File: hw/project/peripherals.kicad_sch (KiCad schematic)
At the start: 72 parts, among them J1 Battery, J10 I2C, J11 Voltage Monitor, J12 Misc, J2 Phases, J3 FTSH-107-01-L-DV-K-A, J4 Throttle, J5 Hall, J6 Serial, J7 SPI, J8 2.54 Comm, J9 CAN, SW3 USER, U3 ATA6561-GAQW-N

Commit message: somewhat organize main groups
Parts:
- renumbered R44 to R38, R45 to R39, R46 to R40, R47 to R41, R48 to R42, R49 to R43, R50 to R44, R51 to R45, R52 to R46, R53 to R47, R54 to R48, R55 to R49, R56 to R50, R57 to R51, R58 to R52, R59 to R53, R60 to R54, R61 to R55, R62 to R56, R63 to R57, R64 to R58, R65 to R59, R66 to R60, R67 to R61, R68 to R62, R69 to R63
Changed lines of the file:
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@@
 		(dnp no)
 		(fields_autoplaced yes)
-		(property "Reference" "R48"
+		(property "Reference" "R42"
 			(at 260.35 38.0999 0)
 			(show_name no)
@@
 			(project "esc"
 				(path "/86a17c4d-db96-42a1-af84-d43fe593f4e6/84ea8536-46c8-4cae-8743-a6718dee2882"
-					(reference "R48")
+					(reference "R42")
 					(unit 1)
 				)
@@
 		(dnp no)
 		(fields_autoplaced yes)
-		(property "Reference" "R58"
+		(property "Reference" "R52"
 			(at 246.38 85.0899 0)
 			(show_name no)
@@
 			(project "esc"
 				(path "/86a17c4d-db96-42a1-af84-d43fe593f4e6/84ea8536-46c8-4cae-8743-a6718dee2882"
-					(reference "R58")
+					(reference "R52")
 					(unit 1)
 				)
@@
 		(dnp no)
 		(fields_autoplaced yes)
-		(property "Reference" "R44"
+		(property "Reference" "R38"
 			(at 246.38 30.4799 0)
 			(show_name no)
@@
 			(project "esc"
 				(path "/86a17c4d-db96-42a1-af84-d43fe593f4e6/84ea8536-46c8-4cae-8743-a6718dee2882"
-					(reference "R44")
+					(reference "R38")
 					(unit 1)
 				)
@@
 		(dnp no)
 		(fields_autoplaced yes)
-		(property "Reference" "R67"
+		(property "Reference" "R61"
 			(at 120.65 126.9999 0)
 			(show_name no)
@@
 			(project "esc"
 				(path "/86a17c4d-db96-42a1-af84-d43fe593f4e6/84ea8536-46c8-4cae-8743-a6718dee2882"
-					(reference "R67")
+					(reference "R61")
 					(unit 1)
 				)
@@
 		(dnp no)
 		(fields_autoplaced yes)
-		(property "Reference" "R61"
+		(property "Reference" "R55"
 			(at 288.29 85.0899 0)
 			(show_name no)
@@
 			(project "esc"
 				(path "/86a17c4d-db96-42a1-af84-d43fe593f4e6/84ea8536-46c8-4cae-8743-a6718dee2882"
-					(reference "R61")
+					(reference "R55")
 					(unit 1)
 				)
@@
 		(dnp no)
 		(fields_autoplaced yes)
-		(property "Reference" "R52"
+		(property "Reference" "R46"
 			(at 40.64 67.3099 0)
 			(show_name no)
@@
 			(project "esc"
 				(path "/86a17c4d-db96-42a1-af84-d43fe593f4e6/84ea8536-46c8-4cae-8743-a6718dee2882"
-					(reference "R52")
+					(reference "R46")
 					(unit 1)
 				)
@@
 		(dnp no)
 		(fields_autoplaced yes)
-		(property "Reference" "R53"
+		(property "Reference" "R47"
 			(at 200.66 68.5799 0)
 			(show_name no)
@@
 			(project "esc"
 				(path "/86a17c4d-db96-42a1-af84-d43fe593f4e6/84ea8536-46c8-4cae-8743-a6718dee2882"
-					(reference "R53")
+					(reference "R47")
 					(unit 1)
 				)
@@
 		(dnp no)
 		(fields_autoplaced yes)
-		(property "Reference" "R57"
+		(property "Reference" "R51"
 			(at 63.5 82.5499 0)
 			(show_name no)
@@
 			(project "esc"
 				(path "/86a17c4d-db96-42a1-af84-d43fe593f4e6/84ea8536-46c8-4cae-8743-a6718dee2882"
-					(reference "R57")
+					(reference "R51")
 					(unit 1)
 				)
@@
 		(in_pos_files yes)
 		(dnp no)
-		(property "Reference" "R64"
+		(property "Reference" "R58"
 			(at 65.278 90.17 90)
 			(show_name no)
@@
 			(project "esc"
 				(path "/86a17c4d-db96-42a1-af84-d43fe593f4e6/84ea8536-46c8-4cae-8743-a6718dee2882"
-					(reference "R64")
+					(reference "R58")
 					(unit 1)
 				)
@@
 		(dnp no)
 		(fields_autoplaced yes)
-		(property "Reference" "R50"
+		(property "Reference" "R44"
 			(at 194.31 58.42 90)
 			(show_name no)
@@
 			(project "esc"
 				(path "/86a17c4d-db96-42a1-af84-d43fe593f4e6/84ea8536-46c8-4cae-8743-a6718dee2882"
-					(reference "R50")
+					(reference "R44")
 					(unit 1)
 				)
@@
 		(dnp no)
 		(fields_autoplaced yes)
-		(property "Reference" "R56"
+		(property "Reference" "R50"
 			(at 55.88 82.5499 0)
 			(show_name no)
@@
 			(project "esc"
 				(path "/86a17c4d-db96-42a1-af84-d43fe593f4e6/84ea8536-46c8-4cae-8743-a6718dee2882"
-					(reference "R56")
+					(reference "R50")
 					(unit 1)
 				)
@@
 		(dnp no)
 		(fields_autoplaced yes)
-		(property "Reference" "R60"
+		(property "Reference" "R54"
 			(at 274.32 85.0899 0)
 			(show_name no)
@@
 			(project "esc"
 				(path "/86a17c4d-db96-42a1-af84-d43fe593f4e6/84ea8536-46c8-4cae-8743-a6718dee2882"
-					(reference "R60")
+					(reference "R54")
 					(unit 1)
 				)
@@
 		(dnp no)
 		(fields_autoplaced yes)
-		(property "Reference" "R47"
+		(property "Reference" "R41"
 			(at 274.32 35.5599 0)
 			(show_name no)
@@
 			(project "esc"
 				(path "/86a17c4d-db96-42a1-af84-d43fe593f4e6/84ea8536-46c8-4cae-8743-a6718dee2882"
-					(reference "R47")
+					(reference "R41")
 					(unit 1)
 				)
@@
 		(dnp no)
 		(fields_autoplaced yes)
-		(property "Reference" "R51"
+		(property "Reference" "R45"
 			(at 33.02 67.3099 0)
 			(show_name no)
@@
 			(project "esc"
 				(path "/86a17c4d-db96-42a1-af84-d43fe593f4e6/84ea8536-46c8-4cae-8743-a6718dee2882"
-					(reference "R51")
+					(reference "R45")
 					(unit 1)
 				)
@@
 		(dnp no)
 		(fields_autoplaced yes)
-		(property "Reference" "R55"
+		(property "Reference" "R49"
 			(at 48.26 82.5499 0)
 			(show_name no)
@@
 			(project "esc"
 				(path "/86a17c4d-db96-42a1-af84-d43fe593f4e6/84ea8536-46c8-4cae-8743-a6718dee2882"
-					(reference "R55")
+					(reference "R49")
 					(unit 1)
 				)
@@
 		(dnp no)
 		(fields_autoplaced yes)
-		(property "Reference" "R62"
+		(property "Reference" "R56"
 			(at 358.14 86.3599 0)
 			(show_name no)
@@
 			(project "esc"
 				(path "/86a17c4d-db96-42a1-af84-d43fe593f4e6/84ea8536-46c8-4cae-8743-a6718dee2882"
-					(reference "R62")
+					(reference "R56")
 					(unit 1)
 				)
@@
 		(in_pos_files yes)
 		(dnp no)
-		(property "Reference" "R65"
+		(property "Reference" "R59"
 			(at 65.278 92.71 90)
 			(show_name no)
@@
 			(project "esc"
 				(path "/86a17c4d-db96-42a1-af84-d43fe593f4e6/84ea8536-46c8-4cae-8743-a6718dee2882"
-					(reference "R65")
+					(reference "R59")
 					(unit 1)
 				)
@@
 		(dnp no)
 		(fields_autoplaced yes)
-		(property "Reference" "R54"
+		(property "Reference" "R48"
 			(at 358.14 73.6599 0)
 			(show_name no)
@@
 			(project "esc"
 				(path "/86a17c4d-db96-42a1-af84-d43fe593f4e6/84ea8536-46c8-4cae-8743-a6718dee2882"
-					(reference "R54")
+					(reference "R48")
 					(unit 1)
 				)
@@
 		(dnp no)
 		(fields_autoplaced yes)
-		(property "Reference" "R45"
+		(property "Reference" "R39"
 			(at 260.35 33.0199 0)
 			(show_name no)
@@
 			(project "esc"
 				(path "/86a17c4d-db96-42a1-af84-d43fe593f4e6/84ea8536-46c8-4cae-8743-a6718dee2882"
-					(reference "R45")
+					(reference "R39")
 					(unit 1)
 				)
@@
 		(dnp no)
 		(fields_autoplaced yes)
-		(property "Reference" "R59"
+		(property "Reference" "R53"
 			(at 260.35 85.0899 0)
 			(show_name no)
@@
 			(project "esc"
 				(path "/86a17c4d-db96-42a1-af84-d43fe593f4e6/84ea8536-46c8-4cae-8743-a6718dee2882"
-					(reference "R59")
+					(reference "R53")
 					(unit 1)
 				)
@@
 		(dnp no)
 		(fields_autoplaced yes)
-		(property "Reference" "R68"
+		(property "Reference" "R62"
 			(at 129.54 126.9999 0)
 			(show_name no)
@@
 			(project "esc"
 				(path "/86a17c4d-db96-42a1-af84-d43fe593f4e6/84ea8536-46c8-4cae-8743-a6718dee2882"
-					(reference "R68")
+					(reference "R62")
 					(unit 1)
 				)
@@
 		(dnp no)
 		(fields_autoplaced yes)
-		(property "Reference" "R49"
+		(property "Reference" "R43"
 			(at 246.38 40.6399 0)
 			(show_name no)
@@
 			(project "esc"
 				(path "/86a17c4d-db96-42a1-af84-d43fe593f4e6/84ea8536-46c8-4cae-8743-a6718dee2882"
-					(reference "R49")
+					(reference "R43")
 					(unit 1)
 				)
@@
 		(in_pos_files yes)
 		(dnp no)
-		(property "Reference" "R63"
+		(property "Reference" "R57"
 			(at 65.278 87.63 90)
 			(show_name no)
@@
 			(project "esc"
 				(path "/86a17c4d-db96-42a1-af84-d43fe593f4e6/84ea8536-46c8-4cae-8743-a6718dee2882"
-					(reference "R63")
+					(reference "R57")
 					(unit 1)
 				)
@@
 		(dnp no)
 		(fields_autoplaced yes)
-		(property "Reference" "R69"
+		(property "Reference" "R63"
 			(at 266.7 130.8099 0)
 			(show_name no)
@@
 			(project "esc"
 				(path "/86a17c4d-db96-42a1-af84-d43fe593f4e6/84ea8536-46c8-4cae-8743-a6718dee2882"
-					(reference "R69")
+					(reference "R63")
 					(unit 1)
 				)
@@
 		(dnp no)
 		(fields_autoplaced yes)
-		(property "Reference" "R66"
+		(property "Reference" "R60"
 			(at 269.24 120.65 90)
 			(show_name no)
@@
 			(project "esc"
 				(path "/86a17c4d-db96-42a1-af84-d43fe593f4e6/84ea8536-46c8-4cae-8743-a6718dee2882"
-					(reference "R66")
+					(reference "R60")
 					(unit 1)
 				)
@@
 		(dnp no)
 		(fields_autoplaced yes)
-		(property "Reference" "R46"
+		(property "Reference" "R40"
 			(at 246.38 35.5599 0)
 			(show_name no)
@@
 			(project "esc"
 				(path "/86a17c4d-db96-42a1-af84-d43fe593f4e6/84ea8536-46c8-4cae-8743-a6718dee2882"
-					(reference "R46")
+					(reference "R40")
 					(unit 1)
 				)

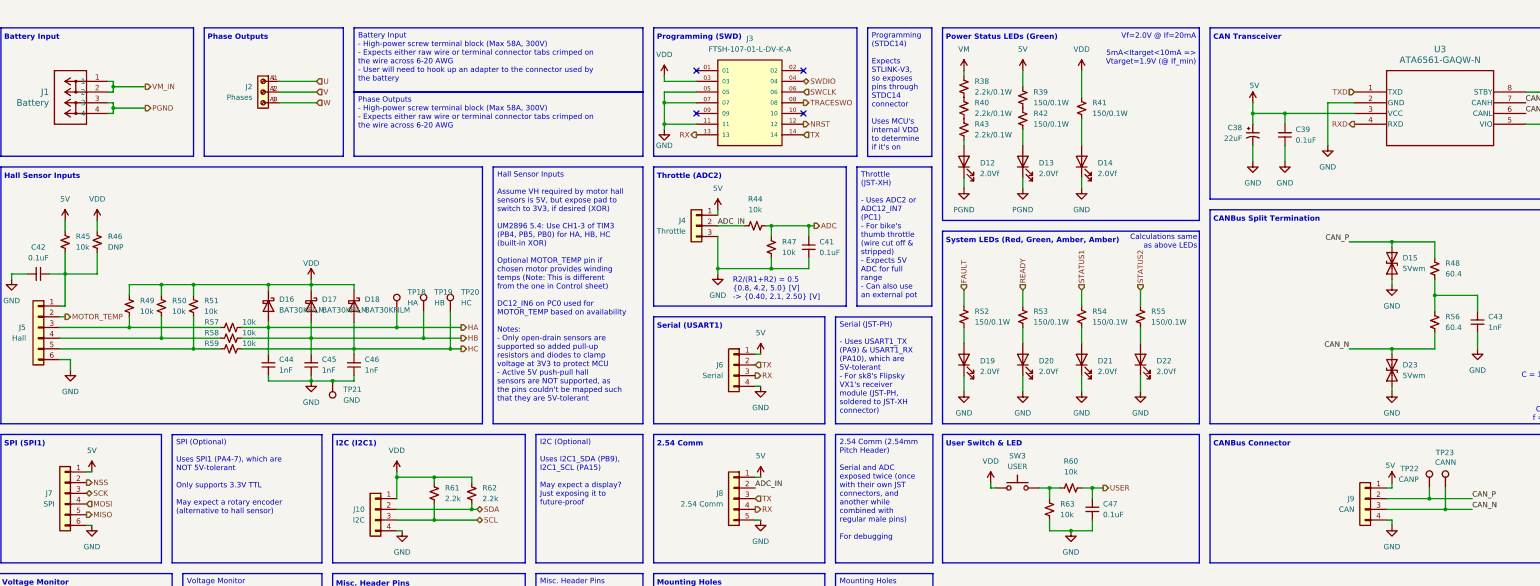
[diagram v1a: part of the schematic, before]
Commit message: Place critical components near MCU
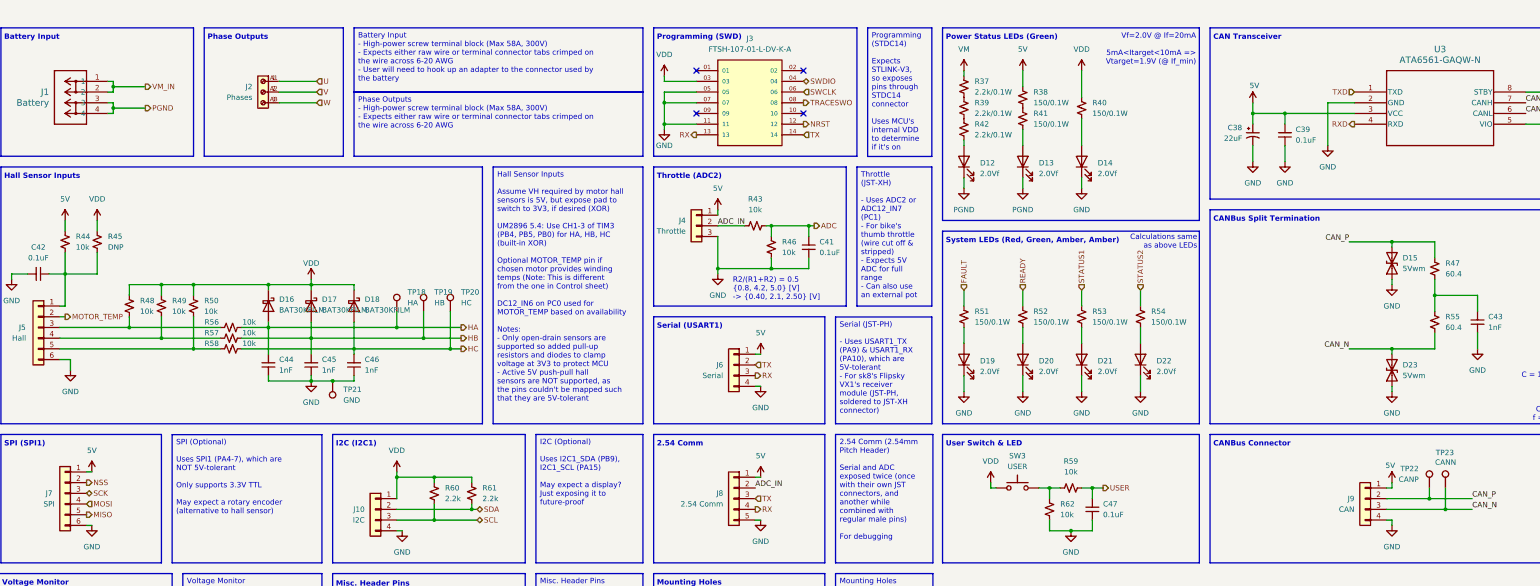
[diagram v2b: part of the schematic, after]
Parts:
- renumbered R38 to R37, R39 to R38, R40 to R39, R41 to R40, R42 to R41, R43 to R42, R44 to R43, R45 to R44, R46 to R45, R47 to R46, R48 to R47, R49 to R48, R50 to R49, R51 to R50, R52 to R51, R53 to R52, R54 to R53, R55 to R54, R56 to R55, R57 to R56, R58 to R57, R59 to R58, R60 to R59, R61 to R60, R62 to R61, R63 to R62
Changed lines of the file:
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@@
 		(dnp no)
 		(fields_autoplaced yes)
-		(property "Reference" "R42"
+		(property "Reference" "R41"
 			(at 260.35 38.0999 0)
 			(show_name no)
@@
 			(project "esc"
 				(path "/86a17c4d-db96-42a1-af84-d43fe593f4e6/84ea8536-46c8-4cae-8743-a6718dee2882"
-					(reference "R42")
+					(reference "R41")
 					(unit 1)
 				)
@@
 		(dnp no)
 		(fields_autoplaced yes)
-		(property "Reference" "R52"
+		(property "Reference" "R51"
 			(at 246.38 85.0899 0)
 			(show_name no)
@@
 			(project "esc"
 				(path "/86a17c4d-db96-42a1-af84-d43fe593f4e6/84ea8536-46c8-4cae-8743-a6718dee2882"
-					(reference "R52")
+					(reference "R51")
 					(unit 1)
 				)
@@
 		(dnp no)
 		(fields_autoplaced yes)
-		(property "Reference" "R38"
+		(property "Reference" "R37"
 			(at 246.38 30.4799 0)
 			(show_name no)
@@
 			(project "esc"
 				(path "/86a17c4d-db96-42a1-af84-d43fe593f4e6/84ea8536-46c8-4cae-8743-a6718dee2882"
-					(reference "R38")
+					(reference "R37")
 					(unit 1)
 				)
@@
 		(dnp no)
 		(fields_autoplaced yes)
-		(property "Reference" "R61"
+		(property "Reference" "R60"
 			(at 120.65 126.9999 0)
 			(show_name no)
@@
 			(project "esc"
 				(path "/86a17c4d-db96-42a1-af84-d43fe593f4e6/84ea8536-46c8-4cae-8743-a6718dee2882"
-					(reference "R61")
+					(reference "R60")
 					(unit 1)
 				)
@@
 		(dnp no)
 		(fields_autoplaced yes)
-		(property "Reference" "R55"
+		(property "Reference" "R54"
 			(at 288.29 85.0899 0)
 			(show_name no)
@@
 			(project "esc"
 				(path "/86a17c4d-db96-42a1-af84-d43fe593f4e6/84ea8536-46c8-4cae-8743-a6718dee2882"
-					(reference "R55")
+					(reference "R54")
 					(unit 1)
 				)
@@
 		(dnp no)
 		(fields_autoplaced yes)
-		(property "Reference" "R46"
+		(property "Reference" "R45"
 			(at 40.64 67.3099 0)
 			(show_name no)
@@
 			(project "esc"
 				(path "/86a17c4d-db96-42a1-af84-d43fe593f4e6/84ea8536-46c8-4cae-8743-a6718dee2882"
-					(reference "R46")
+					(reference "R45")
 					(unit 1)
 				)
@@
 		(dnp no)
 		(fields_autoplaced yes)
-		(property "Reference" "R47"
+		(property "Reference" "R46"
 			(at 200.66 68.5799 0)
 			(show_name no)
@@
 			(project "esc"
 				(path "/86a17c4d-db96-42a1-af84-d43fe593f4e6/84ea8536-46c8-4cae-8743-a6718dee2882"
-					(reference "R47")
+					(reference "R46")
 					(unit 1)
 				)
@@
 		(dnp no)
 		(fields_autoplaced yes)
-		(property "Reference" "R51"
+		(property "Reference" "R50"
 			(at 63.5 82.5499 0)
 			(show_name no)
@@
 			(project "esc"
 				(path "/86a17c4d-db96-42a1-af84-d43fe593f4e6/84ea8536-46c8-4cae-8743-a6718dee2882"
-					(reference "R51")
+					(reference "R50")
 					(unit 1)
 				)
@@
 		(in_pos_files yes)
 		(dnp no)
-		(property "Reference" "R58"
+		(property "Reference" "R57"
 			(at 65.278 90.17 90)
 			(show_name no)
@@
 			(project "esc"
 				(path "/86a17c4d-db96-42a1-af84-d43fe593f4e6/84ea8536-46c8-4cae-8743-a6718dee2882"
-					(reference "R58")
+					(reference "R57")
 					(unit 1)
 				)
@@
 		(dnp no)
 		(fields_autoplaced yes)
-		(property "Reference" "R44"
+		(property "Reference" "R43"
 			(at 194.31 58.42 90)
 			(show_name no)
@@
 			(project "esc"
 				(path "/86a17c4d-db96-42a1-af84-d43fe593f4e6/84ea8536-46c8-4cae-8743-a6718dee2882"
-					(reference "R44")
+					(reference "R43")
 					(unit 1)
 				)
@@
 		(dnp no)
 		(fields_autoplaced yes)
-		(property "Reference" "R50"
+		(property "Reference" "R49"
 			(at 55.88 82.5499 0)
 			(show_name no)
@@
 			(project "esc"
 				(path "/86a17c4d-db96-42a1-af84-d43fe593f4e6/84ea8536-46c8-4cae-8743-a6718dee2882"
-					(reference "R50")
+					(reference "R49")
 					(unit 1)
 				)
@@
 		(dnp no)
 		(fields_autoplaced yes)
-		(property "Reference" "R54"
+		(property "Reference" "R53"
 			(at 274.32 85.0899 0)
 			(show_name no)
@@
 			(project "esc"
 				(path "/86a17c4d-db96-42a1-af84-d43fe593f4e6/84ea8536-46c8-4cae-8743-a6718dee2882"
-					(reference "R54")
+					(reference "R53")
 					(unit 1)
 				)
@@
 		(dnp no)
 		(fields_autoplaced yes)
-		(property "Reference" "R41"
+		(property "Reference" "R40"
 			(at 274.32 35.5599 0)
 			(show_name no)
@@
 			(project "esc"
 				(path "/86a17c4d-db96-42a1-af84-d43fe593f4e6/84ea8536-46c8-4cae-8743-a6718dee2882"
-					(reference "R41")
+					(reference "R40")
 					(unit 1)
 				)
@@
 		(dnp no)
 		(fields_autoplaced yes)
-		(property "Reference" "R45"
+		(property "Reference" "R44"
 			(at 33.02 67.3099 0)
 			(show_name no)
@@
 			(project "esc"
 				(path "/86a17c4d-db96-42a1-af84-d43fe593f4e6/84ea8536-46c8-4cae-8743-a6718dee2882"
-					(reference "R45")
+					(reference "R44")
 					(unit 1)
 				)
@@
 		(dnp no)
 		(fields_autoplaced yes)
-		(property "Reference" "R49"
+		(property "Reference" "R48"
 			(at 48.26 82.5499 0)
 			(show_name no)
@@
 			(project "esc"
 				(path "/86a17c4d-db96-42a1-af84-d43fe593f4e6/84ea8536-46c8-4cae-8743-a6718dee2882"
-					(reference "R49")
+					(reference "R48")
 					(unit 1)
 				)
@@
 		(dnp no)
 		(fields_autoplaced yes)
-		(property "Reference" "R56"
+		(property "Reference" "R55"
 			(at 358.14 86.3599 0)
 			(show_name no)
@@
 			(project "esc"
 				(path "/86a17c4d-db96-42a1-af84-d43fe593f4e6/84ea8536-46c8-4cae-8743-a6718dee2882"
-					(reference "R56")
+					(reference "R55")
 					(unit 1)
 				)
@@
 		(in_pos_files yes)
 		(dnp no)
-		(property "Reference" "R59"
+		(property "Reference" "R58"
 			(at 65.278 92.71 90)
 			(show_name no)
@@
 			(project "esc"
 				(path "/86a17c4d-db96-42a1-af84-d43fe593f4e6/84ea8536-46c8-4cae-8743-a6718dee2882"
-					(reference "R59")
+					(reference "R58")
 					(unit 1)
 				)
@@
 		(dnp no)
 		(fields_autoplaced yes)
-		(property "Reference" "R48"
+		(property "Reference" "R47"
 			(at 358.14 73.6599 0)
 			(show_name no)
@@
 			(project "esc"
 				(path "/86a17c4d-db96-42a1-af84-d43fe593f4e6/84ea8536-46c8-4cae-8743-a6718dee2882"
-					(reference "R48")
+					(reference "R47")
 					(unit 1)
 				)
@@
 		(dnp no)
 		(fields_autoplaced yes)
-		(property "Reference" "R39"
+		(property "Reference" "R38"
 			(at 260.35 33.0199 0)
 			(show_name no)
@@
 			(project "esc"
 				(path "/86a17c4d-db96-42a1-af84-d43fe593f4e6/84ea8536-46c8-4cae-8743-a6718dee2882"
-					(reference "R39")
+					(reference "R38")
 					(unit 1)
 				)
@@
 		(dnp no)
 		(fields_autoplaced yes)
-		(property "Reference" "R53"
+		(property "Reference" "R52"
 			(at 260.35 85.0899 0)
 			(show_name no)
@@
 			(project "esc"
 				(path "/86a17c4d-db96-42a1-af84-d43fe593f4e6/84ea8536-46c8-4cae-8743-a6718dee2882"
-					(reference "R53")
+					(reference "R52")
 					(unit 1)
 				)
@@
 		(dnp no)
 		(fields_autoplaced yes)
-		(property "Reference" "R62"
+		(property "Reference" "R61"
 			(at 129.54 126.9999 0)
 			(show_name no)
@@
 			(project "esc"
 				(path "/86a17c4d-db96-42a1-af84-d43fe593f4e6/84ea8536-46c8-4cae-8743-a6718dee2882"
-					(reference "R62")
+					(reference "R61")
 					(unit 1)
 				)
@@
 		(dnp no)
 		(fields_autoplaced yes)
-		(property "Reference" "R43"
+		(property "Reference" "R42"
 			(at 246.38 40.6399 0)
 			(show_name no)
@@
 			(project "esc"
 				(path "/86a17c4d-db96-42a1-af84-d43fe593f4e6/84ea8536-46c8-4cae-8743-a6718dee2882"
-					(reference "R43")
+					(reference "R42")
 					(unit 1)
 				)
@@
 		(in_pos_files yes)
 		(dnp no)
-		(property "Reference" "R57"
+		(property "Reference" "R56"
 			(at 65.278 87.63 90)
 			(show_name no)
@@
 			(project "esc"
 				(path "/86a17c4d-db96-42a1-af84-d43fe593f4e6/84ea8536-46c8-4cae-8743-a6718dee2882"
-					(reference "R57")
+					(reference "R56")
 					(unit 1)
 				)
@@
 		(dnp no)
 		(fields_autoplaced yes)
-		(property "Reference" "R63"
+		(property "Reference" "R62"
 			(at 266.7 130.8099 0)
 			(show_name no)
@@
 			(project "esc"
 				(path "/86a17c4d-db96-42a1-af84-d43fe593f4e6/84ea8536-46c8-4cae-8743-a6718dee2882"
-					(reference "R63")
+					(reference "R62")
 					(unit 1)
 				)
@@
 		(dnp no)
 		(fields_autoplaced yes)
-		(property "Reference" "R60"
+		(property "Reference" "R59"
 			(at 269.24 120.65 90)
 			(show_name no)
@@
 			(project "esc"
 				(path "/86a17c4d-db96-42a1-af84-d43fe593f4e6/84ea8536-46c8-4cae-8743-a6718dee2882"
-					(reference "R60")
+					(reference "R59")
 					(unit 1)
 				)
@@
 		(dnp no)
 		(fields_autoplaced yes)
-		(property "Reference" "R40"
+		(property "Reference" "R39"
 			(at 246.38 35.5599 0)
 			(show_name no)
@@
 			(project "esc"
 				(path "/86a17c4d-db96-42a1-af84-d43fe593f4e6/84ea8536-46c8-4cae-8743-a6718dee2882"
-					(reference "R40")
+					(reference "R39")
 					(unit 1)
 				)
